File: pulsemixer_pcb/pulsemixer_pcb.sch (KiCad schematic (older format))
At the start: 32 parts, among them SW101 SW_PUSH_SPST, SW102 SW_PUSH_SPST, SW103 SW_PUSH_SPST, U101 SN74LHC08DR, U102 SN74HC21DR, U103 74LVC3G17

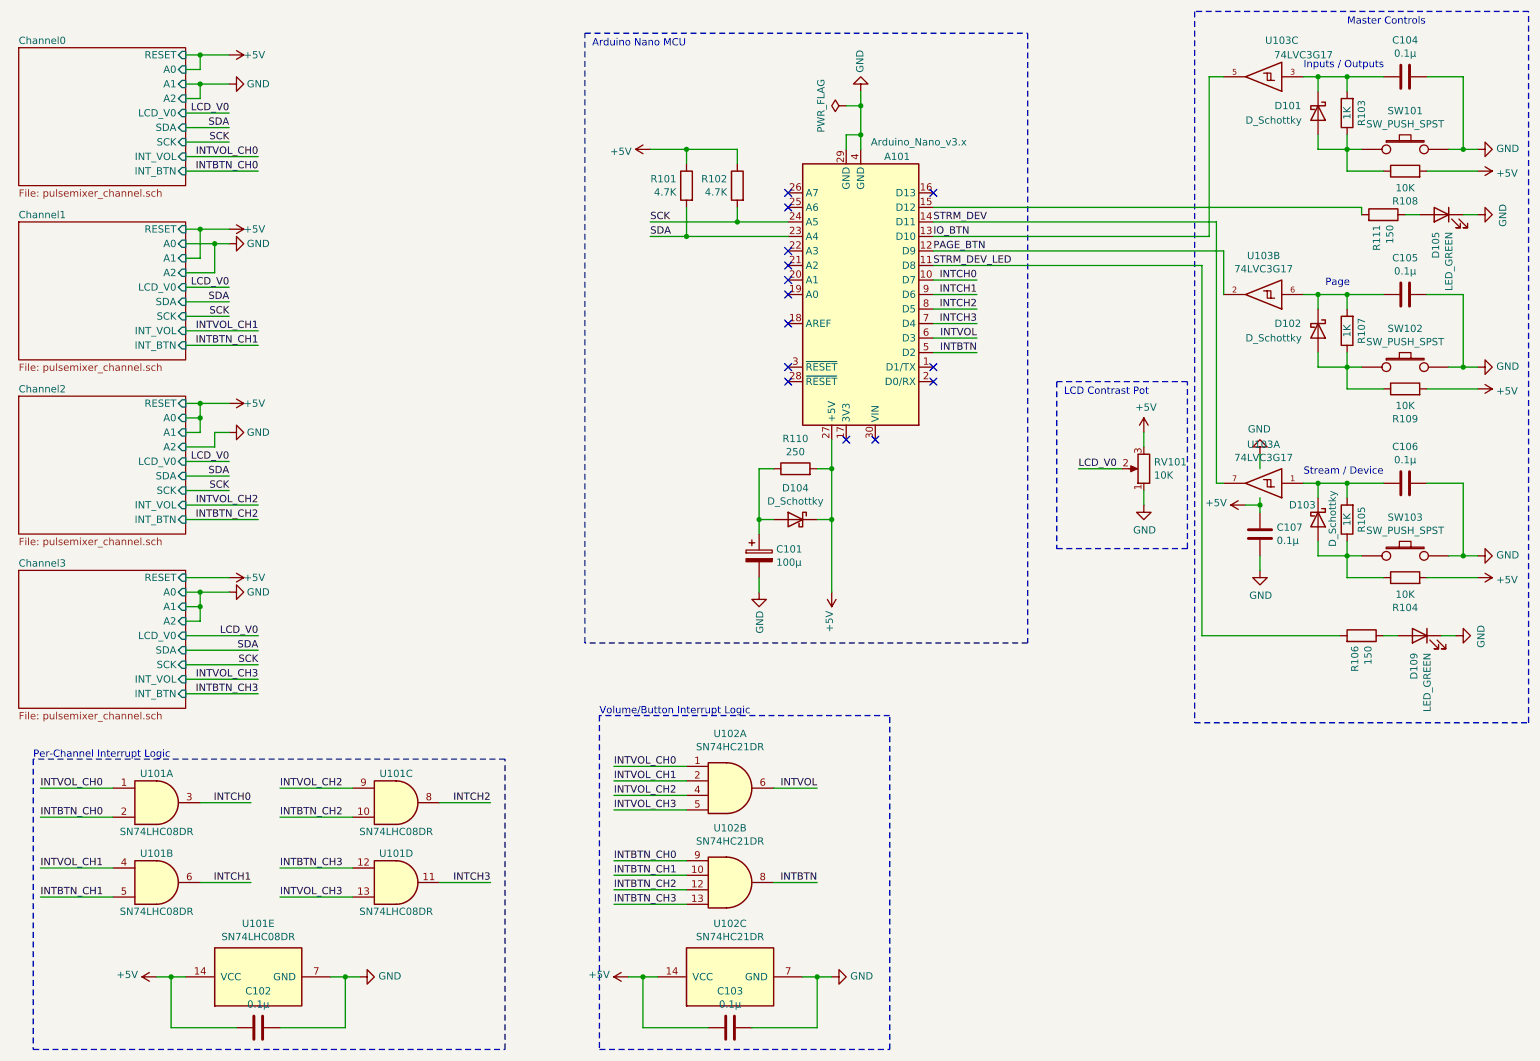
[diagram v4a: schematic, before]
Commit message: Added another AND gate to include master section buttons in the buttn interrupt logic.
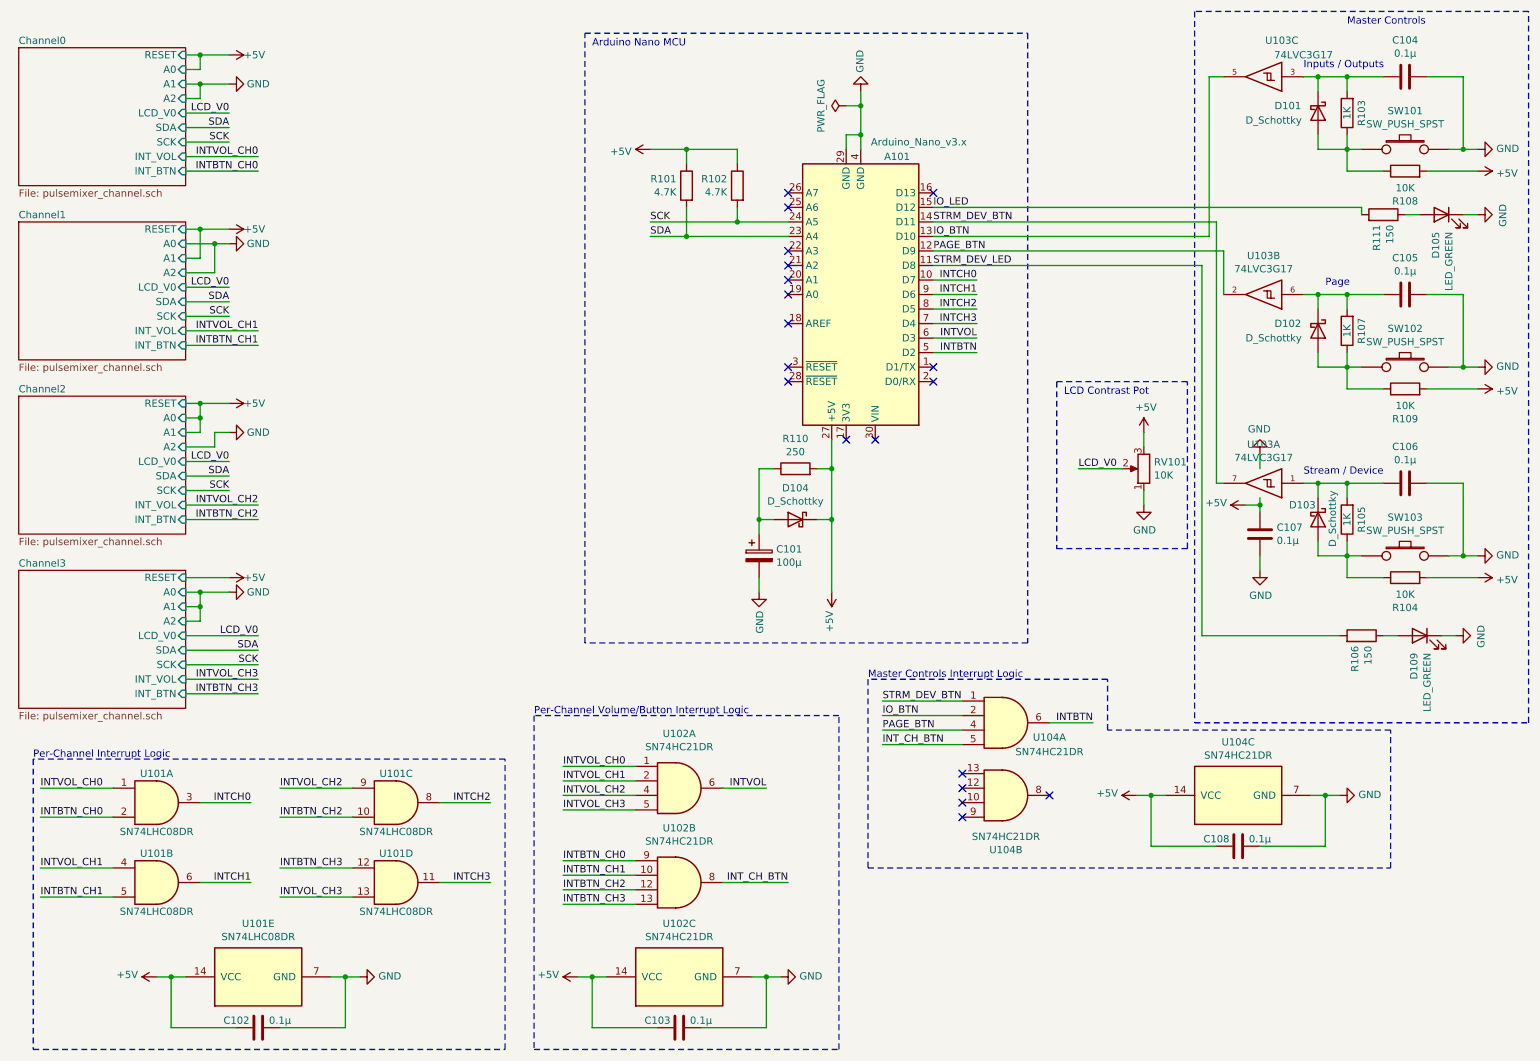
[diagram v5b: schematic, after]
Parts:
- added C108: 0.1µ, Capacitors_SMD:C_0805_HandSoldering, symbol Device:C
- added U104: SN74HC21DR, Housings_SOIC:SOIC-14_3.9x8.7mm_Pitch1.27mm, symbol pulsemixer_pcb:SN74HC21DR
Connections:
- net +5V: now also C108.2, U104.14 (VCC)
- net GND: now also C108.1, U104.7 (GND)
- net INTBTN: now also U104.6; no longer U102.8
- net IO_BTN: now also U104.2
- net PAGE_BTN: now also U104.4
- net IO_LED: now reaches A101.15 (D12), R111.2
- net STRM_DEV renamed STRM_DEV_BTN
- net STRM_DEV_BTN: now also U104.1
- new net INT_CH_BTN: U102.8, U104.5
- no-connect marks 14 -> 19
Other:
- note added: "Master Controls Interrupt Logic"
- note added: "Per-Channel Volume/Button Interrupt Logic"
- note removed: "Volume/Button Interrupt Logic"
- moved on the sheet: C103, U102A, U102B, U102C

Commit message: Finalized changes to board and sent for fabrication.
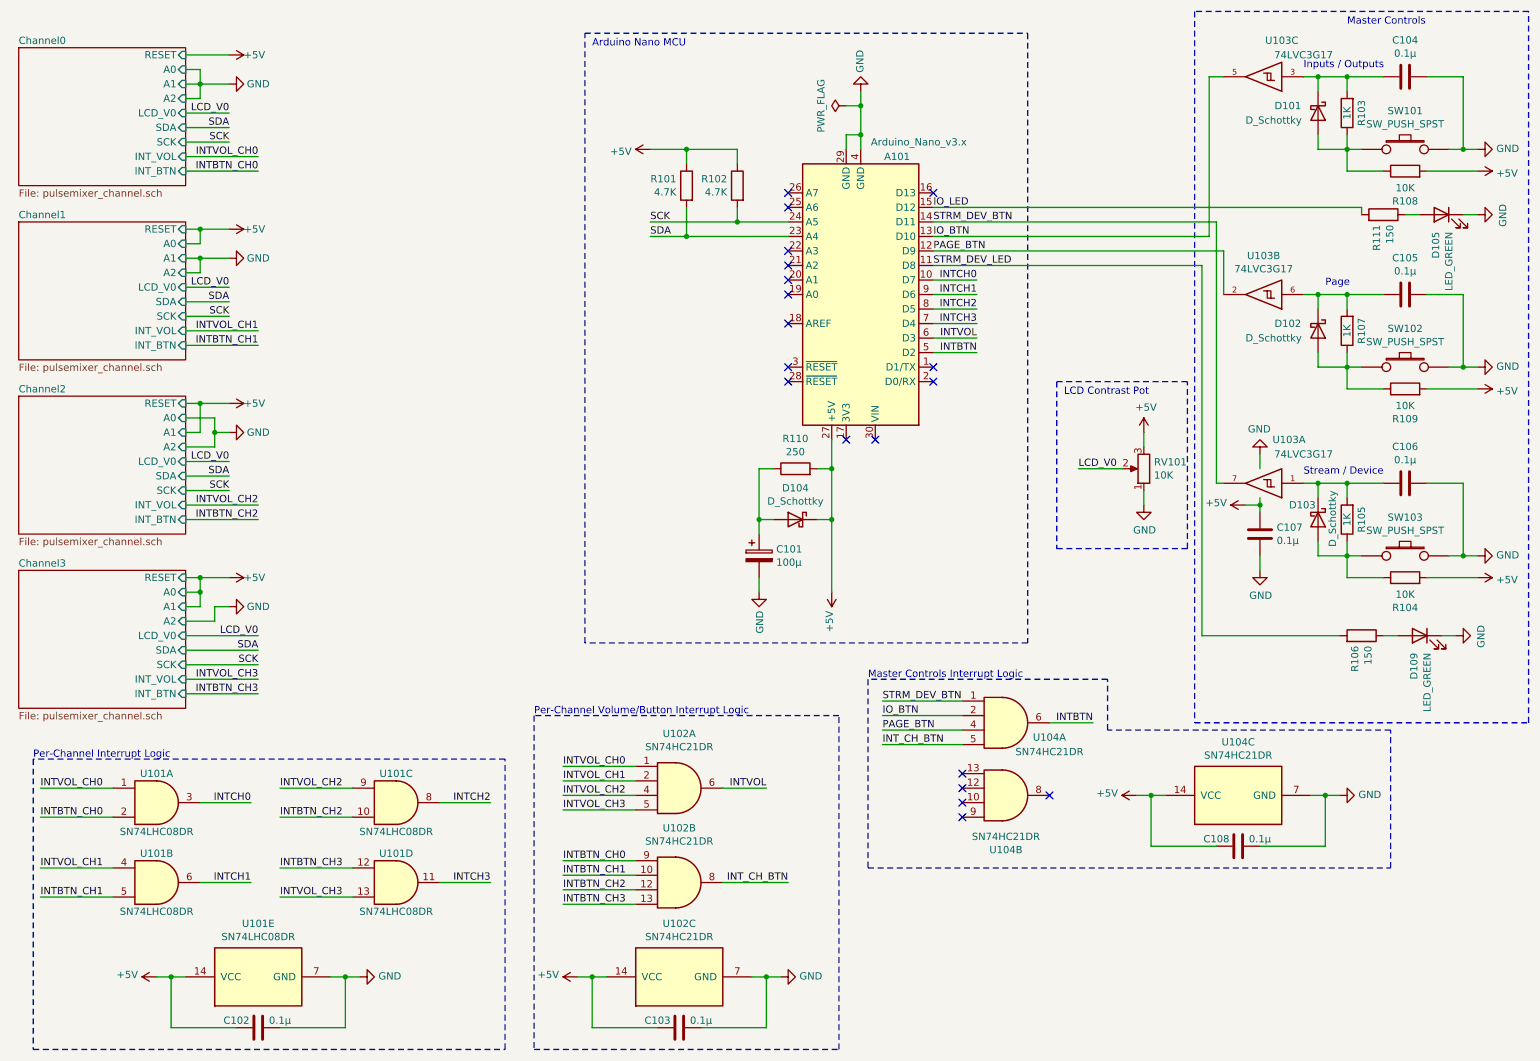
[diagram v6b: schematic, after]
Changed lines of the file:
@@
 L power:GND #PWR0102
 U 1 1 5F0452C1
-P 2200 4600
-F 0 "#PWR0102" H 2200 4350 50  0001 C CNN
-F 1 "GND" V 2200 4400 50  0000 C CNN
-F 2 "" H 2200 4600 50  0001 C CNN
-F 3 "" H 2200 4600 50  0001 C CNN
-	1    2200 4600
-	0    -1   -1   0
-$EndComp
-Wire Wire Line
-	2200 4600 2000 4600
-Wire Wire Line
-	2000 4800 1900 4800
+P 2200 4700
+F 0 "#PWR0102" H 2200 4450 50  0001 C CNN
+F 1 "GND" V 2200 4500 50  0000 C CNN
+F 2 "" H 2200 4700 50  0001 C CNN
+F 3 "" H 2200 4700 50  0001 C CNN
+	1    2200 4700
+	0    -1   -1   0
+$EndComp
 Wire Wire Line
 	1900 4700 2000 4700
-Connection ~ 2000 4700
-Wire Wire Line
-	2000 4700 2000 4800
 Wire Wire Line
 	1900 4600 2000 4600
-Connection ~ 2000 4600
 Wire Wire Line
 	2000 4600 2000 4700
 Wire Wire Line
-	1900 4500 2200 4500
+	1900 4500 2000 4500
 Wire Wire Line
 	1900 4900 2400 4900
@@
 L power:GND #PWR0106
 U 1 1 5F077D3A
-P 2200 2200
-F 0 "#PWR0106" H 2200 1950 50  0001 C CNN
-F 1 "GND" V 2200 2000 50  0000 C CNN
-F 2 "" H 2200 2200 50  0001 C CNN
-F 3 "" H 2200 2200 50  0001 C CNN
-	1    2200 2200
+P 2200 2300
+F 0 "#PWR0106" H 2200 2050 50  0001 C CNN
+F 1 "GND" V 2200 2100 50  0000 C CNN
+F 2 "" H 2200 2300 50  0001 C CNN
+F 3 "" H 2200 2300 50  0001 C CNN
+	1    2200 2300
 	0    -1   -1   0
 $EndComp
 Wire Wire Line
 	1900 2300 2000 2300
-Wire Wire Line
-	1900 2100 2000 2100
 Wire Wire Line
 	1900 2500 2200 2500
@@
 	1900 3500 2000 3500
 Wire Wire Line
-	1900 3400 2000 3400
-Wire Wire Line
-	2000 3400 2000 3500
-Wire Wire Line
 	1900 3300 2000 3300
 Wire Wire Line
@@
 $EndComp
 Wire Wire Line
-	1900 2200 2100 2200
-Wire Wire Line
-	2100 2400 2100 2200
-Wire Wire Line
-	1900 2400 2100 2400
-Connection ~ 2100 2200
-Wire Wire Line
-	2000 2300 2000 2100
-Connection ~ 2000 2100
-Wire Wire Line
-	2000 2100 2200 2100
-Wire Wire Line
-	2100 2200 2200 2200
-Wire Wire Line
-	2000 3400 2000 3300
-Connection ~ 2000 3400
+	2000 2400 2000 2300
+Wire Wire Line
+	1900 2400 2000 2400
 Connection ~ 2000 3300
 Wire Wire Line
@@
 U 1 1 5F24E174
 P 9300 3850
-F 0 "U103" H 9275 3583 50  0000 C CNN
-F 1 "74LVC3G17" H 9275 3674 50  0000 C CNN
+F 0 "U103" H 9100 3550 50  0000 C CNN
+F 1 "74LVC3G17" H 9000 3650 50  0000 C CNN
 F 2 "Housings_SSOP:SSOP-8_2.95x2.8mm_Pitch0.65mm" H 9300 3850 50  0001 C CNN
 F 3 "http://www.ti.com/lit/sg/scyt129e/scyt129e.pdf" H 9300 3850 50  0001 C CNN
@@
 	2000 1100 2200 1100
 Wire Wire Line
-	2000 900  2200 900
-Connection ~ 2000 900
-Wire Wire Line
-	2000 1000 2000 900
-Wire Wire Line
 	1900 1000 2000 1000
 $Comp
@@
 Wire Wire Line
 	1900 1300 2200 1300
-Wire Wire Line
-	1900 900  2000 900
 Wire Wire Line
 	2000 1100 2000 1200
@@
 Text Notes 6600 5200 0    50   ~ 0
 Master Controls Interrupt Logic
+Wire Wire Line
+	1900 900  2200 900
+Wire Wire Line
+	2000 1000 2000 1100
+Wire Wire Line
+	1900 2100 2000 2100
+Connection ~ 2000 2300
+Wire Wire Line
+	2000 2300 2200 2300
+Wire Wire Line
+	1900 2200 2000 2200
+Wire Wire Line
+	2000 2200 2000 2100
+Connection ~ 2000 2100
+Wire Wire Line
+	2000 2100 2200 2100
+Wire Wire Line
+	2000 3300 2000 3500
+Wire Wire Line
+	1900 3400 2100 3400
+Wire Wire Line
+	2100 3400 2100 3500
+Connection ~ 2100 3500
+Wire Wire Line
+	2000 4600 2000 4500
+Connection ~ 2000 4600
+Connection ~ 2000 4500
+Wire Wire Line
+	2000 4500 2200 4500
+Wire Wire Line
+	2100 4800 2100 4700
+Wire Wire Line
+	2100 4700 2200 4700
+Wire Wire Line
+	1900 4800 2100 4800
 $EndSCHEMATC
